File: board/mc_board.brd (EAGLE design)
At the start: 38 x 25.1 mm, 15 parts, among them IC1 MEGA8-P, Q1 16MHz

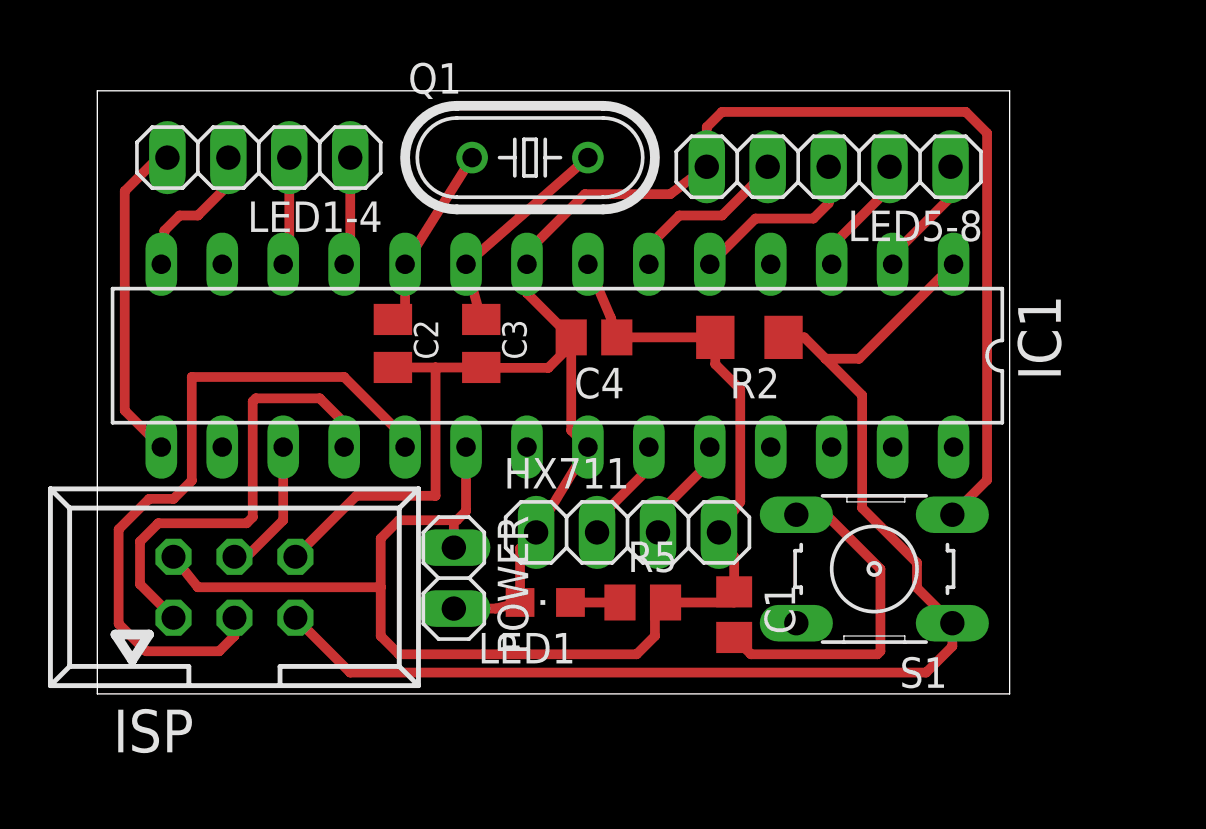
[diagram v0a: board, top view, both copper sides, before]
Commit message: added UART pins to layout
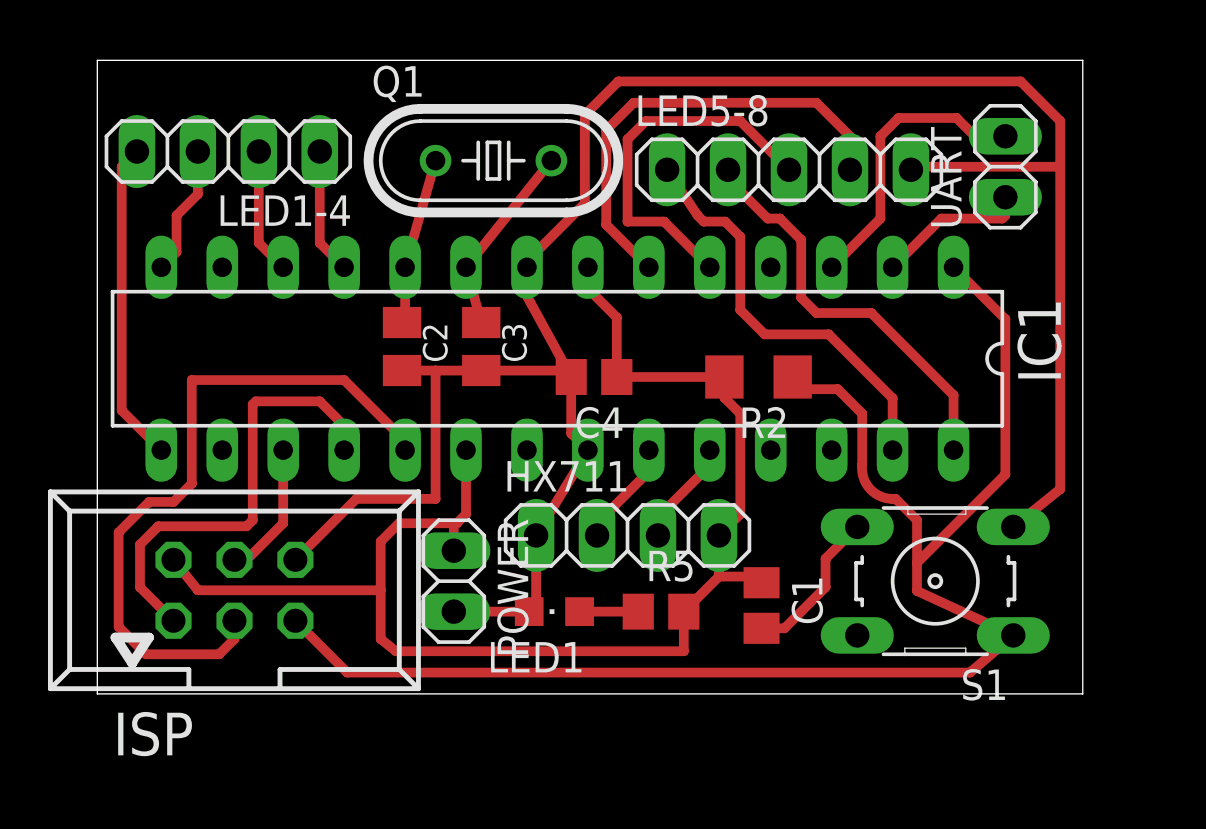
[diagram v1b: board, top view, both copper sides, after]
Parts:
- added UART: JP2, pinhead:1X02
- moved S1 2.59 mm to (34.9, 4.70)
- moved R2 1.69 mm to (27.6, 13.2)
- moved LED5-8 1.66 mm to (28.8, 21.8), turned to 0 degrees
- moved C4 1.65 mm to (20.7, 13.2)
- moved Q1 1.53 mm to (16.5, 22.2)
- moved LED1-4 1.30 mm to (5.46, 22.6)
- moved C1 1.20 mm to (27.7, 3.68)
- moved R5 0.85 mm to (23.5, 3.43)
- moved LED1 0.54 mm to (19.1, 3.43)
- moved C2 0.40 mm to (12.7, 14.5)
- moved C3 0.13 mm to (16.0, 14.5)
- moved ISP 0.13 mm to (5.71, 4.32)
- moved HX711 0.13 mm to (22.1, 6.60)
- moved POWER 0.13 mm to (14.9, 4.70)
- moved IC1 0.13 mm to (19.2, 14.0)
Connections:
- removed net PC4: IC1.27
- removed net PC5: IC1.28
- removed net PD0/LED5: IC1.2, LED5-8.1
- removed net PD1/LED6: IC1.3, LED5-8.2
- new net PC4/LED5: IC1.27, LED5-8.1
- new net PC5/LED6: IC1.28, LED5-8.2
- new net PD0/UART: IC1.2, UART.1
- new net PD1/UART: IC1.3, UART.2
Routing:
- net PC4/LED5: track 0.00 -> 17.5 mm
- net PC5/LED6: track 0.00 -> 17.2 mm
- net PD1/UART: track 0.00 -> 12.1 mm
- net GND: track 79.1 -> 91.1 mm
- net PD4/LED8: track 7.16 -> 19.1 mm
- net RESET: track 52.0 -> 62.5 mm
- net PD3/LED7: track 7.53 -> 15.5 mm
- net N$9: track 14.3 -> 6.44 mm
- net PD0/UART: track 0.00 -> 6.36 mm
- net PD1/LED6: track 5.06 -> 0.00 mm
- net PD0/LED5: track 5.06 -> 0.00 mm
- net N$5: track 9.14 -> 8.08 mm
- net N$6: track 8.35 -> 7.43 mm
- net +5V: track 57.2 -> 58.1 mm
- net PB0/LED3: track 6.05 -> 5.46 mm
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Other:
- board size 38 x 25.1 mm -> 41.1 x 26.4 mm

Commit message: tweaked board layout, defined pins in led.c accordingly
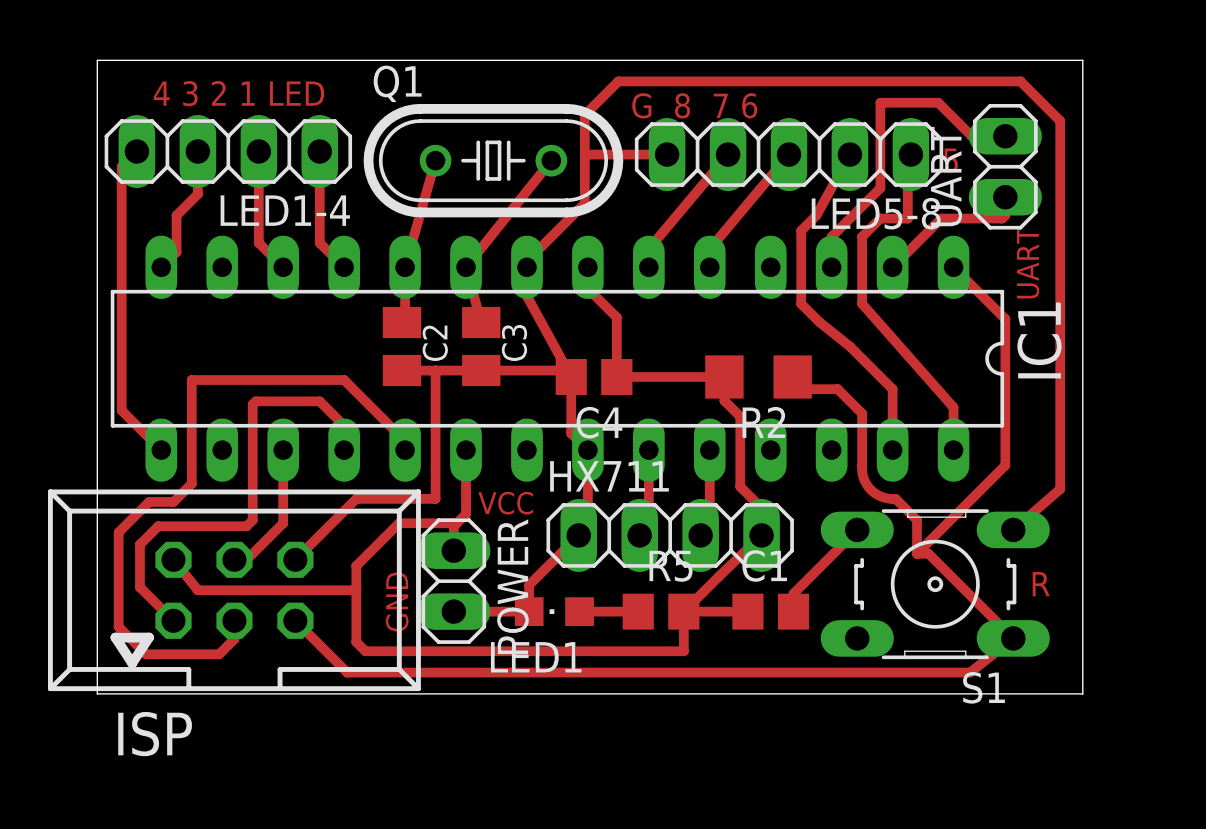
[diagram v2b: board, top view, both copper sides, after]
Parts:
- moved HX711 1.78 mm to (23.9, 6.60)
- moved LED5-8 0.63 mm to (28.8, 22.5), turned to 180 degrees
- moved C1 0.46 mm to (28.1, 3.43), turned to 0 degrees
- moved S1 0.13 mm to (34.9, 4.57)
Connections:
- removed net PC4/LED5: IC1.27, LED5-8.1
- removed net PC5/LED6: IC1.28, LED5-8.2
- new net PC4/LED6: IC1.27, LED5-8.2
- new net PC5/LED5: IC1.28, LED5-8.1
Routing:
- net PC4/LED5: track 17.5 -> 0.00 mm
- net PC5/LED6: track 17.2 -> 0.00 mm
- net PC5/LED5: track 0.00 -> 15.3 mm
- net PC4/LED6: track 0.00 -> 14.6 mm
- net PD4/LED8: track 19.1 -> 5.90 mm
- net PD3/LED7: track 15.5 -> 5.90 mm
- net GND: track 91.1 -> 88.5 mm
- net +5V: track 58.1 -> 60.2 mm
- net N$9: track 6.44 -> 4.50 mm
- net PD1/UART: track 12.1 -> 13.5 mm
- net RESET: track 62.5 -> 61.5 mm
- net PC1/SCK: track 4.45 -> 3.71 mm
- net PC0/DT: track 4.45 -> 3.71 mm
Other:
- board text added: "4 3 2 1 LED"
- board text added: "5"
- board text added: "G 8 7 6"
- board text added: "GND"
- board text added: "R"
- board text added: "UART"
- board text added: "VCC"

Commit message: improved board layout
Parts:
- removed LED5-8: JP2, pinhead:1X05
- added GND: Gnd, pinhead:1X01
- added LED5-8JO: JP2, pinhead:1X04
- moved UART 2.82 mm to (35.1, 22.4)
- moved LED1-4 1.53 mm to (5.33, 21.1)
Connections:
- net GND: now also GND.1; no longer LED5-8.5
- net PC4/LED6: now also LED5-8JO.2; no longer LED5-8.2
- net PC5/LED5: now also LED5-8JO.1; no longer LED5-8.1
- net PD3/LED7: now also LED5-8JO.3; no longer LED5-8.3
- net PD4/LED8: now also LED5-8JO.4; no longer LED5-8.4
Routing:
- net GND: track 88.5 -> 80.7 mm
- net PD1/UART: track 13.5 -> 8.35 mm
- net PC4/LED6: track 14.6 -> 17.0 mm
- net PD0/UART: track 6.36 -> 3.99 mm
- net PD4/LED8: track 5.90 -> 3.82 mm
- net PD3/LED7: track 5.90 -> 3.82 mm
- net PB0/LED3: track 5.46 -> 3.88 mm
- net PB1/LED4: track 13.4 -> 11.8 mm
- net PD6/LED2: track 5.25 -> 3.78 mm
- net PD5/LED1: track 5.25 -> 3.78 mm
- net RESET: track 61.5 -> 60.6 mm
- net PC5/LED5: track 15.3 -> 16.0 mm
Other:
- board size 41.1 x 26.4 mm -> 40.4 x 26 mm
- board text added: "8 7 6 5"
- board text added: "G"
- board text removed: "5"
- board text removed: "G 8 7 6"

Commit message: even better board layout
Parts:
- moved POWER 20.0 mm to (24.9, 22.0), turned to 0 degrees
- moved UART 17.6 mm to (28.2, 6.10), turned to 180 degrees
- moved R2 10.4 mm to (37.8, 15.0)
- moved LED5-8JO 5.37 mm to (32.8, 22.0)
- moved HX711 3.72 mm to (20.2, 6.10)
- moved GND 3.43 mm to (40.0, 21.0)
- moved C1 3.18 mm to (24.9, 3.30)
- moved R5 2.80 mm to (20.7, 3.30)
- moved LED1 2.16 mm to (16.9, 3.30)
- moved C4 1.65 mm to (19.2, 13.8), turned to 90 degrees
- moved S1 1.35 mm to (35.9, 3.68)
- moved ISP 1.30 mm to (6.99, 4.57)
- moved IC1 1.30 mm to (20.4, 14.2)
- moved C2 1.17 mm to (13.8, 14.7)
- moved LED1-4 0.52 mm to (5.21, 21.6)
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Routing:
- net +5V: track 60.2 -> 87.8 mm
- net PD0/UART: track 3.99 -> 19.2 mm
- net RESET: track 60.6 -> 49.9 mm
- net PD1/UART: track 8.35 -> 15.0 mm
- net GND: track 80.7 -> 86.9 mm
- net PC0/DT: track 3.71 -> 7.35 mm
- net PC1/SCK: track 3.71 -> 7.17 mm
- net N$9: track 4.50 -> 7.92 mm
- net PD3/LED7: track 3.82 -> 6.78 mm
- net PD4/LED8: track 3.82 -> 6.70 mm
- net PC4/LED6: track 17.0 -> 15.2 mm
- net PC5/LED5: track 16.0 -> 14.7 mm
- net N$6: track 7.43 -> 6.35 mm
- net N$5: track 8.08 -> 7.15 mm
- net PD6/LED2: track 3.78 -> 4.65 mm
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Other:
- board size 40.4 x 26 mm -> 41.8 x 25 mm
- board text added: "Gnd"
- board text added: "ISP"
- board text added: "Rst"
- board text removed: "8 7 6 5"
- board text removed: "G"
- board text removed: "GND"
- board text removed: "R"
- board text removed: "VCC"

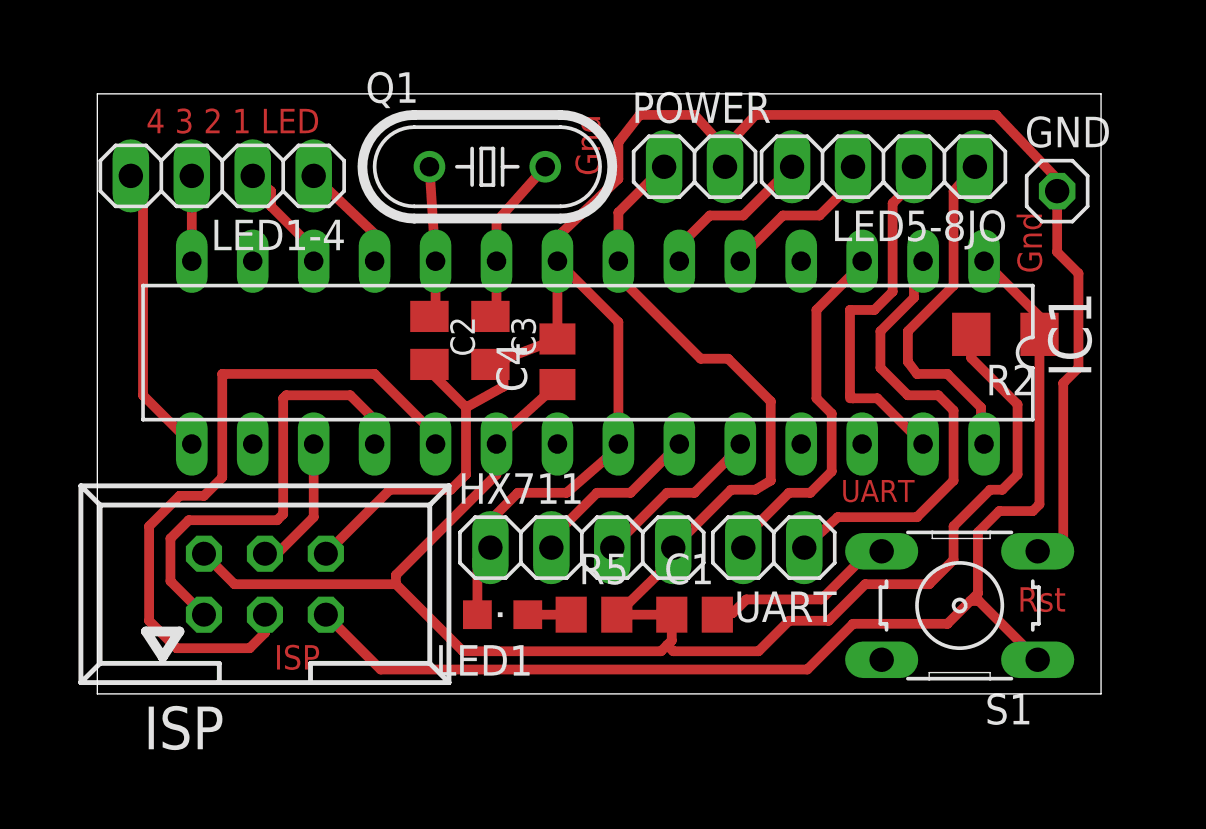
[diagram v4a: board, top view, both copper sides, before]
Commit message: removed gnd pin form board
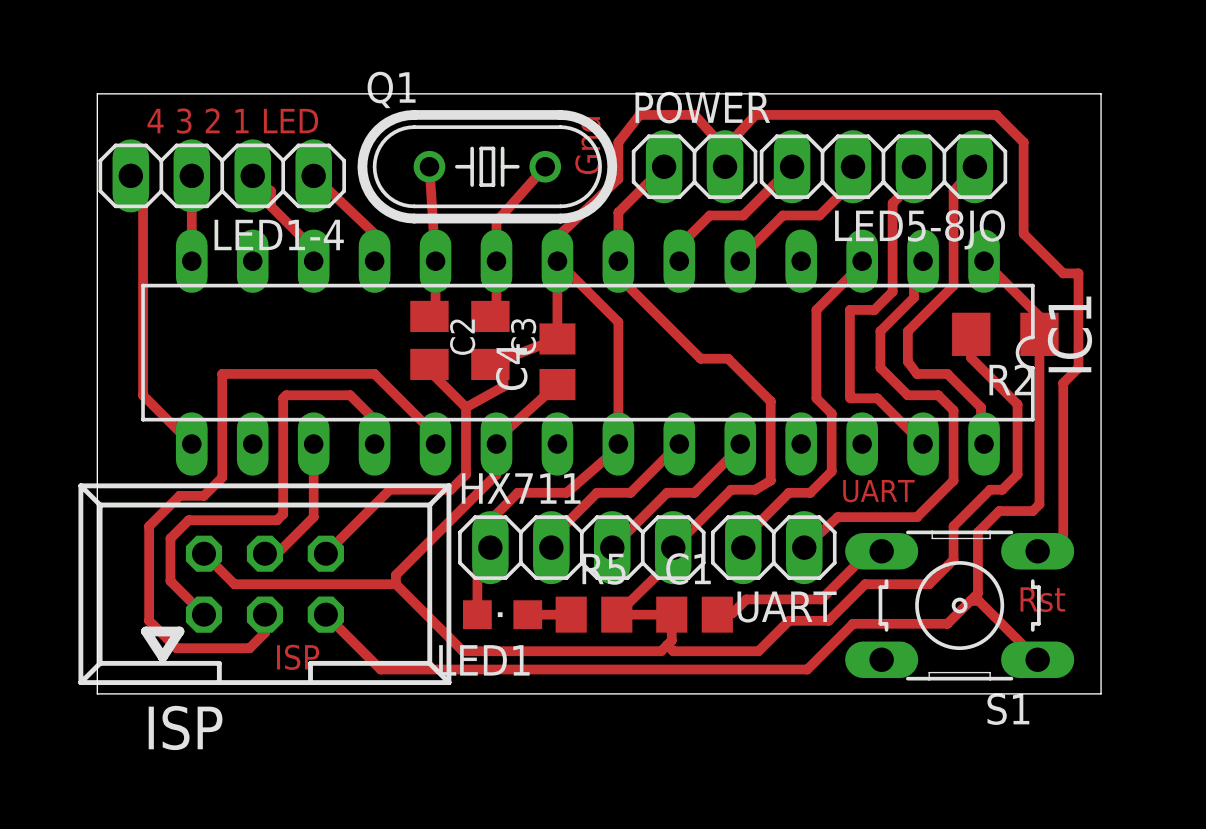
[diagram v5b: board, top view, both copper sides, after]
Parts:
- removed GND: Gnd, pinhead:1X01
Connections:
- net GND: no longer GND.1
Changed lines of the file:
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@@
 <text x="30.988" y="8.001" size="0.9144" layer="1" font="vector" ratio="28">UART</text>
 <text x="38.354" y="3.429" size="1.016" layer="1" font="vector" ratio="28">Rst</text>
-<text x="39.37" y="17.526" size="1.016" layer="1" font="vector" ratio="28" rot="R90">Gnd</text>
 <text x="20.955" y="21.59" size="1.016" layer="1" font="vector" ratio="28" rot="R90">Gnd</text>
 <text x="7.366" y="1.016" size="1.016" layer="1" font="vector" ratio="28">ISP</text>
@@
 <element name="LED1-4" library="pinhead" package="1X04" value="JP3" x="5.207" y="21.59" rot="R180"/>
 <element name="UART" library="pinhead" package="1X02" value="JP2" x="28.194" y="6.096" rot="R180"/>
-<element name="GND" library="pinhead" package="1X01" value="Gnd" x="40.005" y="20.955"/>
 <element name="LED5-8JO" library="pinhead" package="1X04" value="JP2" x="32.766" y="21.971" rot="R180"/>
 </elements>
@@
 <contactref element="POWER" pad="2"/>
 <contactref element="HX711" pad="1"/>
-<contactref element="GND" pad="1"/>
 <wire x1="9.525" y1="5.842" x2="12.192" y2="8.509" width="0.4064" layer="1"/>
 <wire x1="12.192" y1="8.509" x2="14.732" y2="8.509" width="0.4064" layer="1"/>
@@
 <wire x1="40.259" y1="12.954" x2="40.894" y2="13.589" width="0.4064" layer="1"/>
 <wire x1="40.894" y1="13.589" x2="40.894" y2="17.526" width="0.4064" layer="1"/>
-<wire x1="40.894" y1="17.526" x2="40.005" y2="18.415" width="0.4064" layer="1"/>
-<wire x1="40.005" y1="18.415" x2="40.005" y2="20.955" width="0.4064" layer="1"/>
-<wire x1="40.005" y1="20.955" x2="40.005" y2="21.463" width="0.4064" layer="1"/>
-<wire x1="40.005" y1="21.463" x2="37.465" y2="24.13" width="0.4064" layer="1"/>
 <wire x1="37.465" y1="24.13" x2="27.432" y2="24.13" width="0.4064" layer="1"/>
 <wire x1="27.432" y1="24.13" x2="26.035" y2="22.606" width="0.4064" layer="1"/>
@@
 <wire x1="21.717" y1="21.463" x2="19.177" y2="19.05" width="0.4064" layer="1"/>
 <wire x1="19.177" y1="19.05" x2="19.177" y2="18.034" width="0.4064" layer="1"/>
+<wire x1="40.894" y1="17.526" x2="40.259" y2="17.526" width="0.4064" layer="1"/>
+<wire x1="40.259" y1="17.526" x2="38.608" y2="19.177" width="0.4064" layer="1"/>
+<wire x1="38.608" y1="19.177" x2="38.608" y2="22.987" width="0.4064" layer="1"/>
+<wire x1="38.608" y1="22.987" x2="37.465" y2="24.13" width="0.4064" layer="1"/>
 </signal>
 <signal name="+5V">
@@
 <contactref element="LED1-4" pad="4"/>
 <wire x1="3.937" y1="10.414" x2="1.905" y2="12.446" width="0.4064" layer="1"/>
-<wire x1="1.651" y1="21.209" x2="1.905" y2="20.955" width="0.4064" layer="1"/>
-<wire x1="1.905" y1="20.955" x2="1.905" y2="12.446" width="0.4064" layer="1"/>
-<wire x1="1.651" y1="21.209" x2="1.397" y2="21.59" width="0" layer="19" extent="1-1"/>
+<wire x1="1.905" y1="21.082" x2="1.905" y2="12.446" width="0.4064" layer="1"/>
+<wire x1="1.905" y1="21.082" x2="1.397" y2="21.59" width="0.4064" layer="1"/>
 </signal>
 <signal name="PD5/LED1">

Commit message: changed reset button to normal button
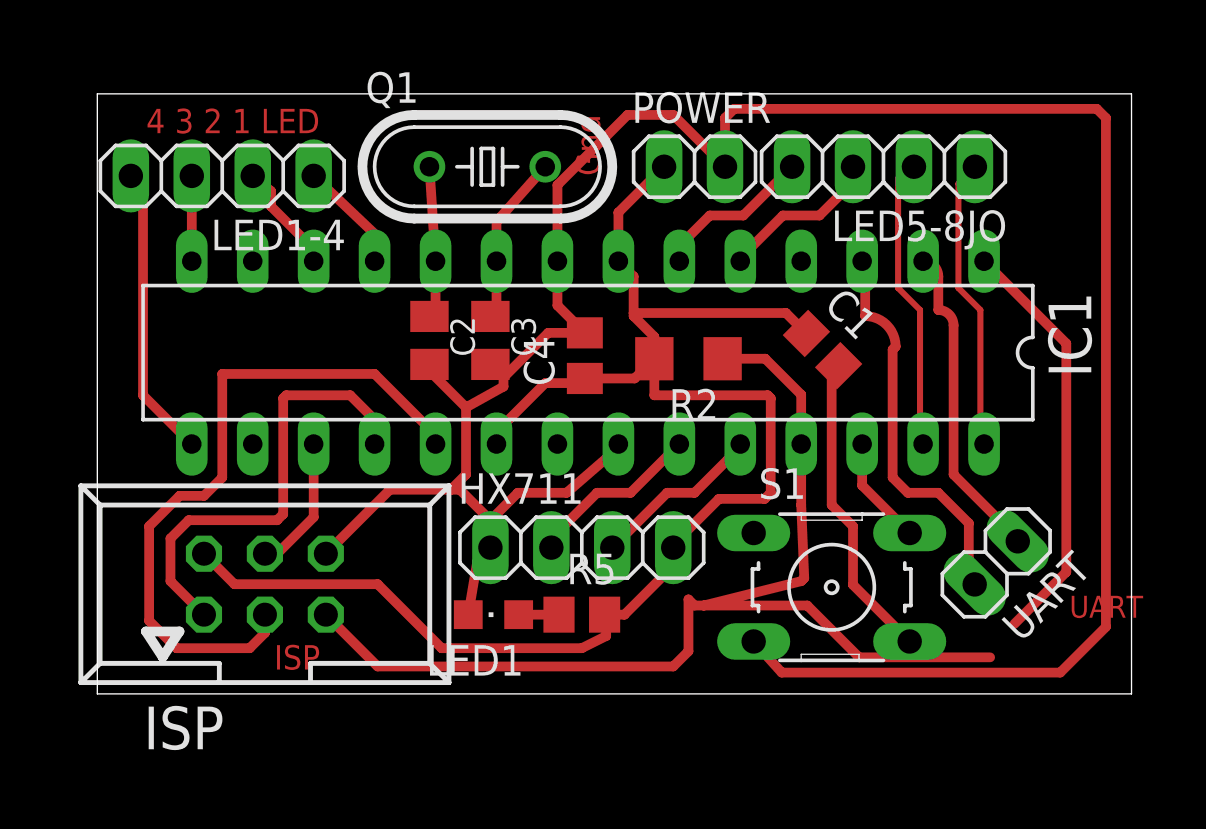
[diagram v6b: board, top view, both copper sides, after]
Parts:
- moved R2 13.2 mm to (24.6, 14.0)
- moved C1 12.3 mm to (30.2, 14.4), turned to 315 degrees
- moved UART 9.29 mm to (37.5, 5.46), turned to 225 degrees
- moved S1 5.39 mm to (30.6, 4.45), turned to 0 degrees
- moved C4 1.17 mm to (20.3, 14.1)
- moved R5 0.51 mm to (20.2, 3.30)
- moved LED1 0.38 mm to (16.5, 3.30)
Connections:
- net PC3: now also S1.2
- net RESET: no longer S1.1
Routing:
- net +5V: track 87.8 -> 65.2 mm
- net GND: track 87.3 -> 103.7 mm
- net RESET: track 49.9 -> 65.3 mm
- net PD0/UART: track 19.2 -> 13.3 mm
- net N$9: track 7.92 -> 13.6 mm
- net PC3: track 0.00 -> 4.53 mm
- net PC4/LED6: track 15.2 -> 12.4 mm
- net PC5/LED5: track 14.7 -> 12.3 mm
- net PD1/UART: track 15.0 -> 16.3 mm
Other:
- board size 41.8 x 25 mm -> 43.1 x 25 mm
- board text removed: "Rst"
